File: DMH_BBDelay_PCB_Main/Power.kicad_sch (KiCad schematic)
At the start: 13 parts, among them J0 Conn_01x01, J100 IDC_02x05, J101 IDC_02x08

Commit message: Schematic in progress
Next is implementation of Channel B, CV Linking and Ping-Pong mode
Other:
- title: Power Distribution -> 3205 Delay
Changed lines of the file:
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@@
 	(paper "A4")
 	(title_block
-		(title "Power Distribution")
+		(title "3205 Delay")
 		(company "DMH Instruments")
 		(comment 1 "PCB for 10cm Kosmo format synthesizer module")

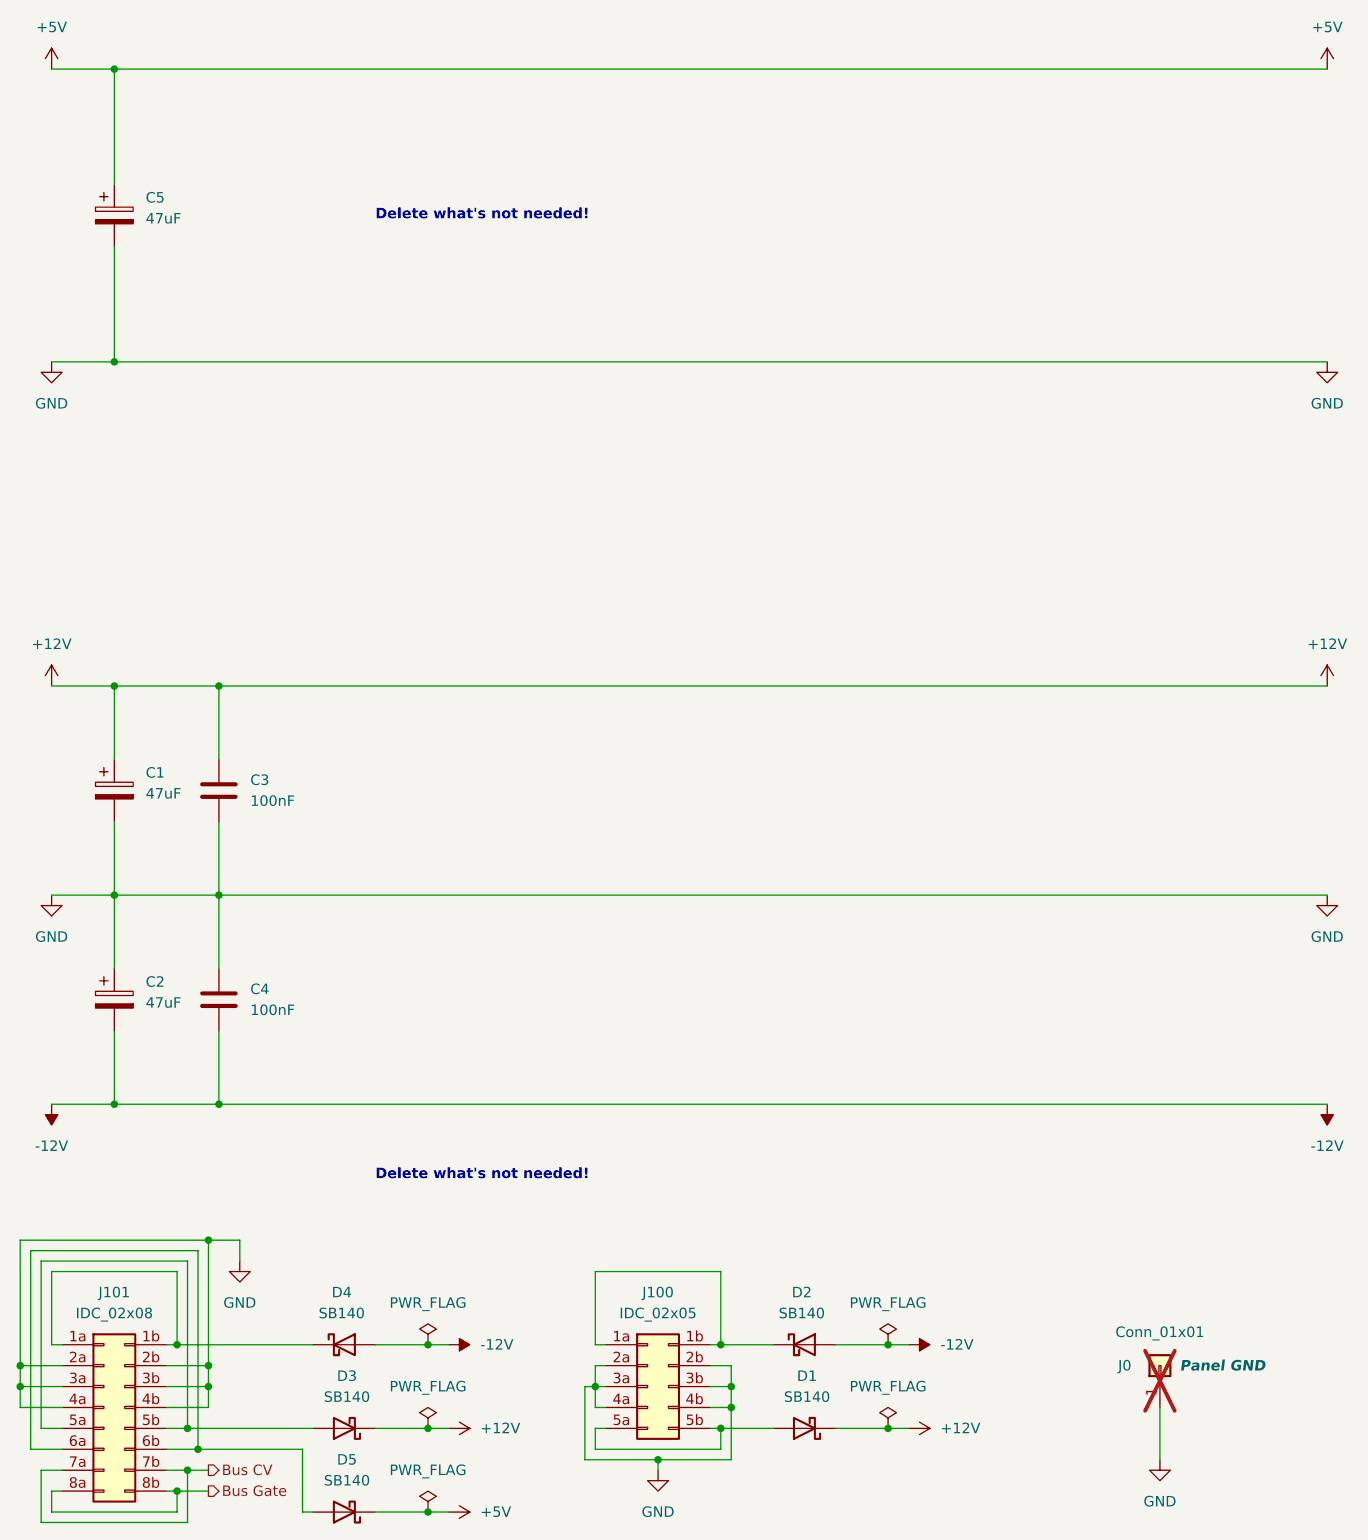
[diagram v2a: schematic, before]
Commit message: Implemented tone control
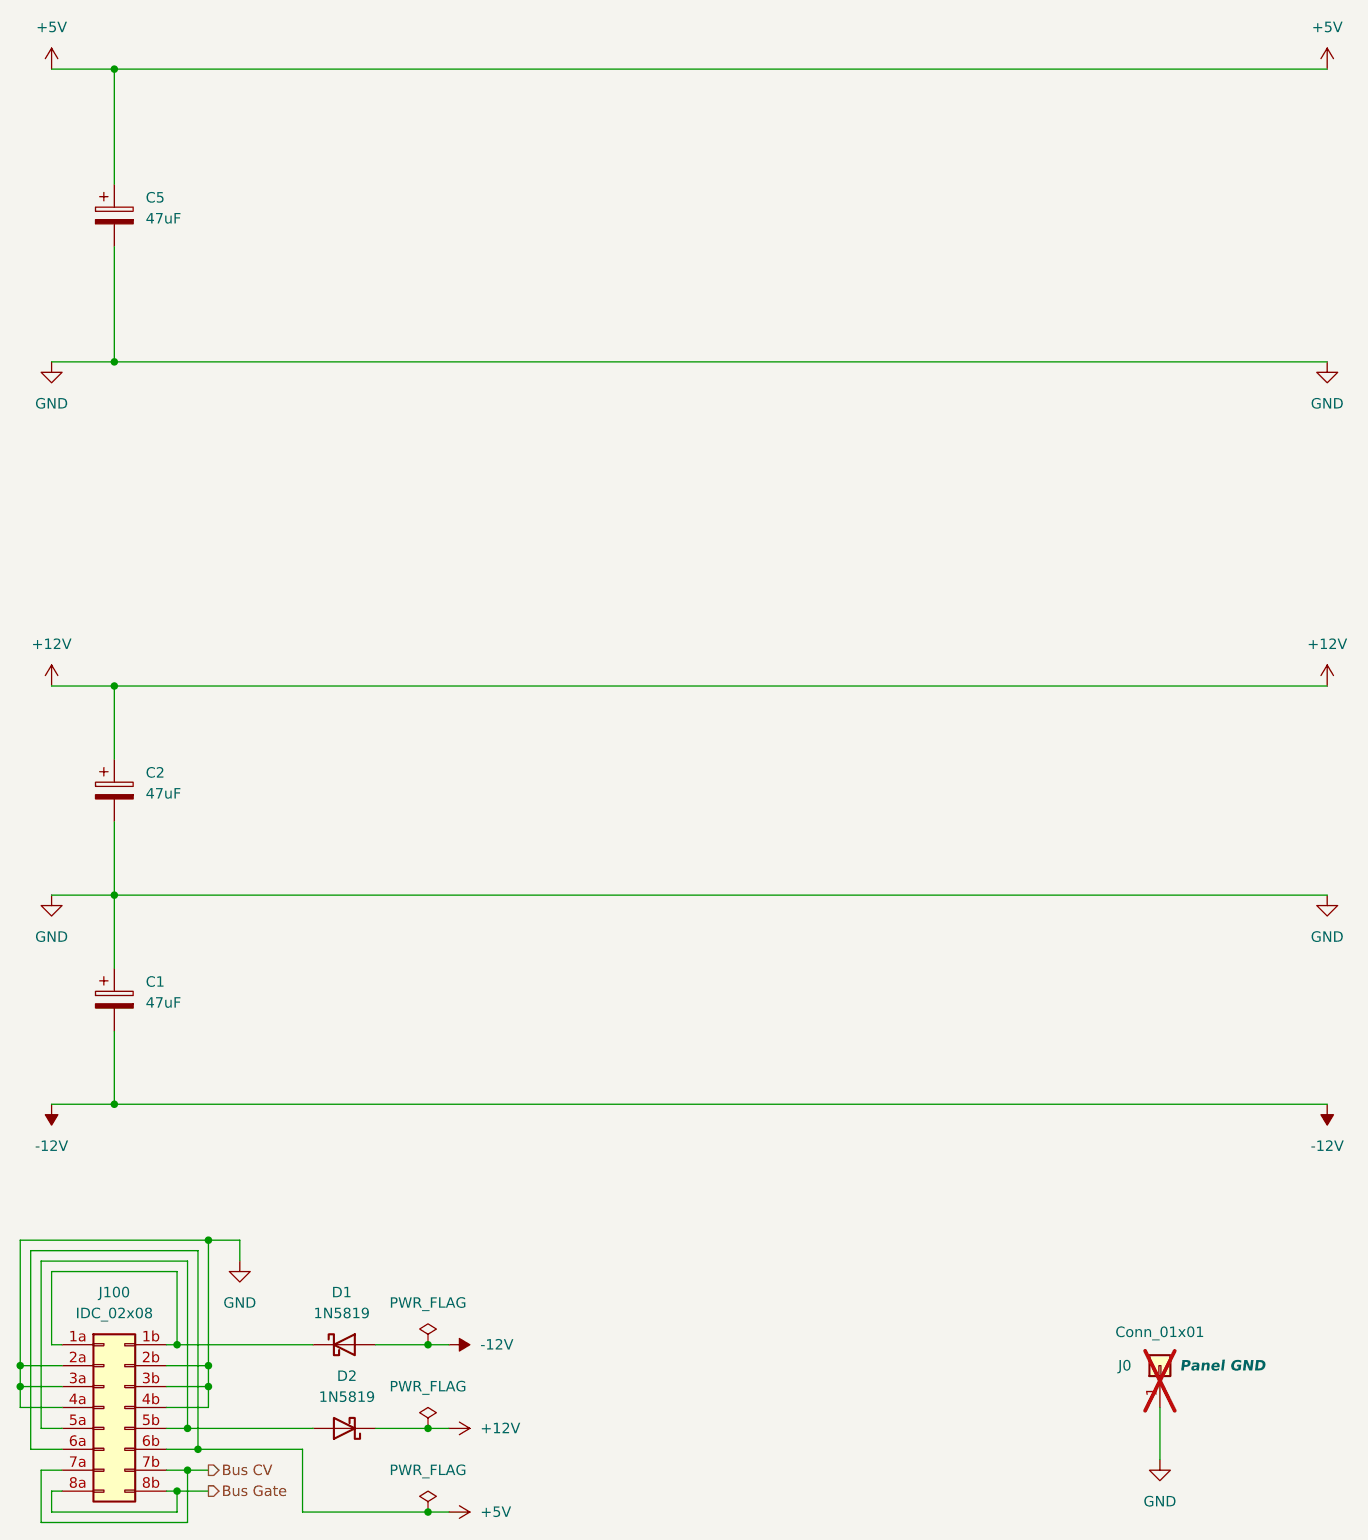
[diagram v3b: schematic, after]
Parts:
- removed C3, C4: 100nF, Capacitor_THT:C_Disc_D4.3mm_W1.9mm_P5.00mm, symbol Device:C
- removed D1, D2, D5: SB140, Diode_THT:D_DO-41_SOD81_P10.16mm_Horizontal, symbol Diode:SB140
- removed J100: IDC_02x05, SynthStuff:IDC-Header_2x05_P2.54mm_Vertical_Eurorack, symbol SynthStuff:Eurorack_Power_Connector_10Pin
- D1: renamed from D4; value SB140 -> 1N5819; symbol Diode:SB140 -> Diode:1N5819
- D2: renamed from D3; value SB140 -> 1N5819; symbol Diode:SB140 -> Diode:1N5819
- renumbered C2 to C1, C1 to C2, J101 to J100
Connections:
- net +5V: now also J100.6a (Pin_6a), J100.6b (Pin_6b)
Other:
- note removed: "Delete what's not needed!"
